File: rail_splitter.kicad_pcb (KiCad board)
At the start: 2 copper layers, 100 x 85 mm, 82 parts, among them J1 input -, J2 input +, J3 gnd load, J6 -load, J8 +load, Q11 AO3401A, Q12 AO3401A, Q13 BD909, Q14 BD910, Q15 MMBT5551L, Q16 MMBT5551L, Q17 MMBT5551L, Q3 MMBT5551L, Q5 MMBT5551L, Q6 AO3400A, Q7 AO3400A, Q8 MMBT5401, SW1 SW_DPDT_x2, SW2 SW_Push, U1 OP07, U2 NE5532, U3 NE5532, U4 LM2936-3.3, U5 NE5532

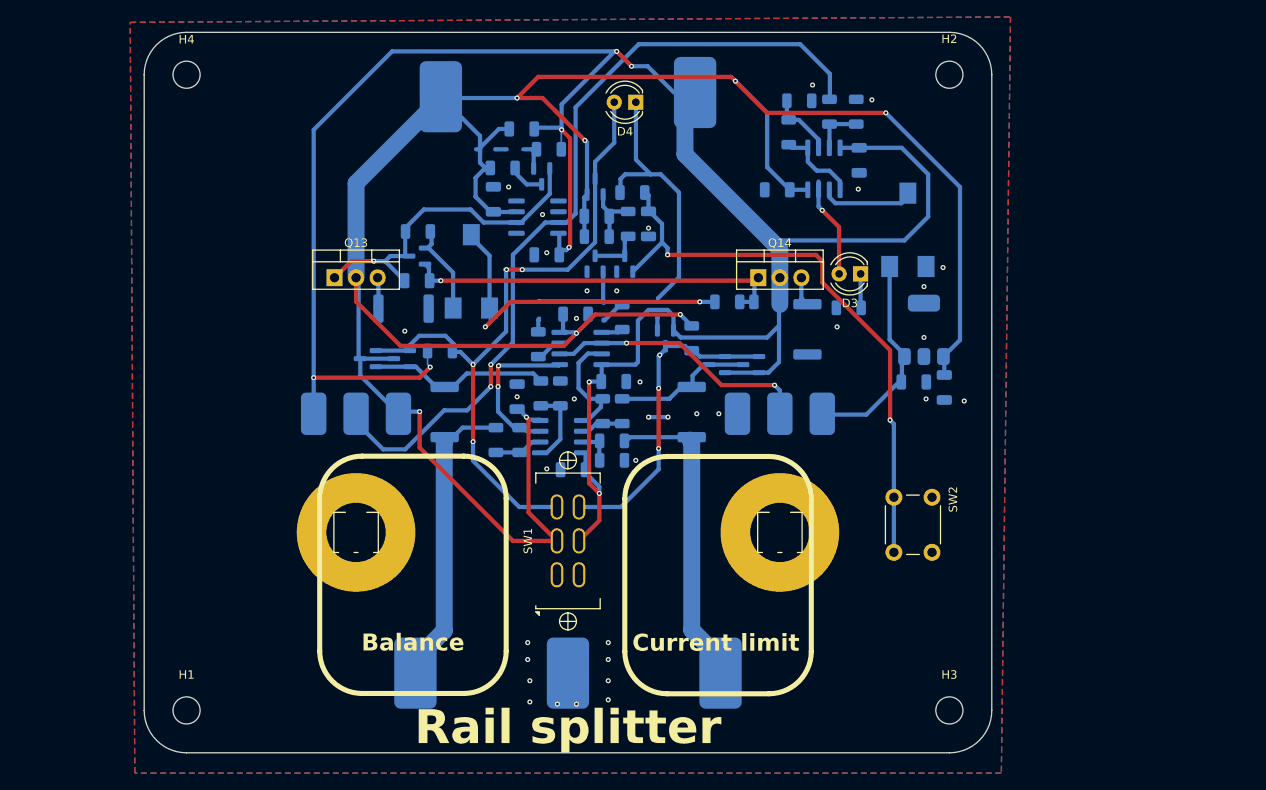
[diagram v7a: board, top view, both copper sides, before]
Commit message: moving things around, rounded tracks
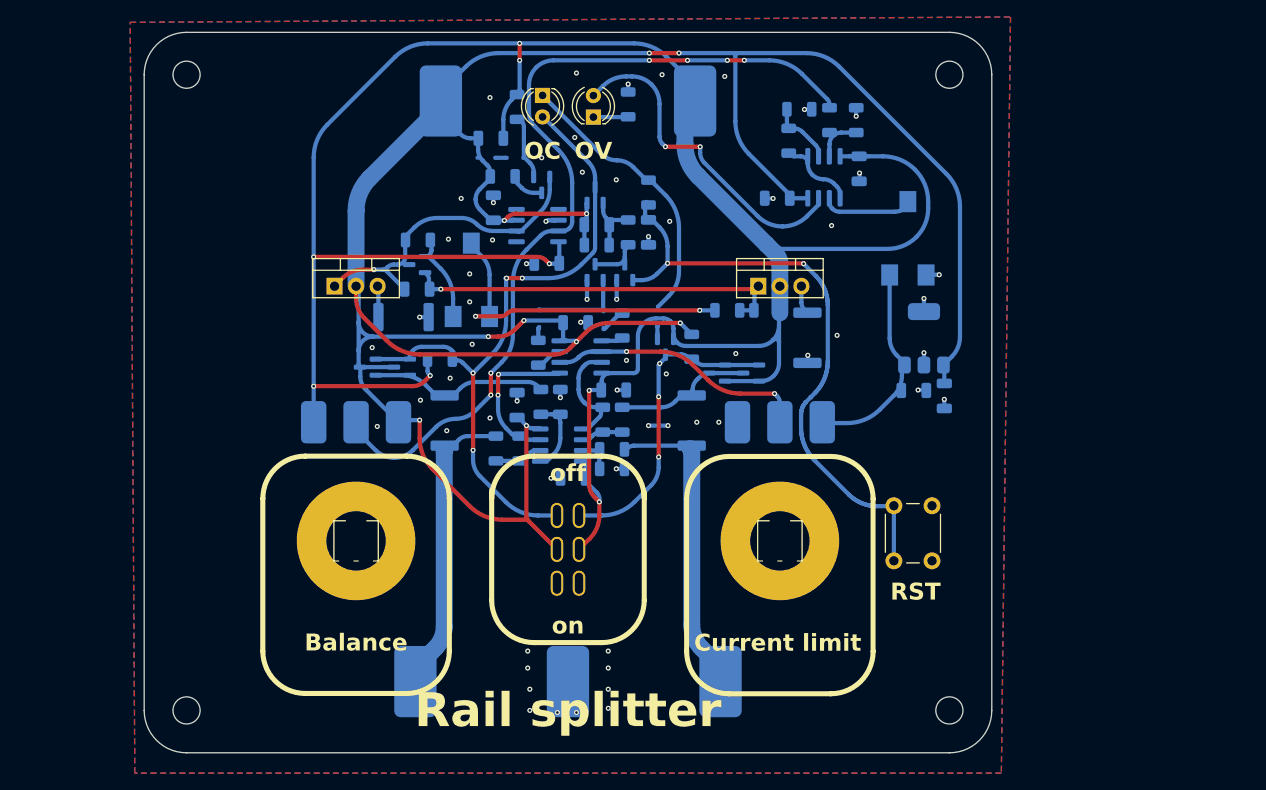
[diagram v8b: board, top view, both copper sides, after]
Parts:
- moved D3 36.6 mm to (103.0, 75.0), turned to 90 degrees
- moved R10 35.4 mm to (107.1, 73.5), turned to 90 degrees
- moved D4 11.0 mm to (97.0, 72.4), turned to -90 degrees
- moved R5 6.25 mm to (94.0, 73.8), turned to 90 degrees
- moved C1 3.81 mm to (90.9, 77.5)
- moved R17 1.90 mm to (109.5, 83.9), turned to -90 degrees
- moved C10 1.00 mm to (105.4, 107.2)
- moved C11 1.00 mm to (103.4, 87.7)
- moved C12 1.00 mm to (140.8, 107.2)
- moved C15 1.00 mm to (94.0, 109.0)
- moved C16 1.00 mm to (100.6, 117.6)
- moved C17 1.00 mm to (109.5, 88.6)
- moved C2 1.00 mm to (82.2, 95.3)
- moved C3 1.00 mm to (124.7, 84.6)
- moved C4 1.00 mm to (134.4, 81.1)
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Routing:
- net Net-(D3-A): track 11.9 -> 39.1 mm, vias 1 -> 2
- net GND: track 0.00 -> 24.3 mm, vias 34 -> 62
- net INPUT+: track 300.8 -> 311.3 mm, vias 8 -> 10
- net /GND_SET: track 96.7 -> 102.6 mm, vias 2 -> 6
- net Net-(D2-K): track 3.95 -> 7.29 mm
- net Net-(Q17-B): track 69.5 -> 72.7 mm
- net INPUT-: track 274.8 -> 276.9 mm
- net Net-(R8-Pad1): track 39.5 -> 38.4 mm
- net Net-(Q13-B): track 38.3 -> 37.3 mm
- net enable+: track 80.4 -> 79.4 mm
- net Net-(D4-K): track 32.4 -> 33.4 mm
- net CURR_LIMIT: track 31.7 -> 31.0 mm
- net Net-(U2B-+): track 9.81 -> 9.08 mm
- net Net-(U2A-+): track 5.96 -> 5.31 mm
- net Net-(U5A-+): track 13.2 -> 12.5 mm
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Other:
- board text added: "OC"
- board text added: "OV"
- board text added: "RST"
- board text added: "off"
- board text added: "on"
